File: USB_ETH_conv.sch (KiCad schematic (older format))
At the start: 20 parts

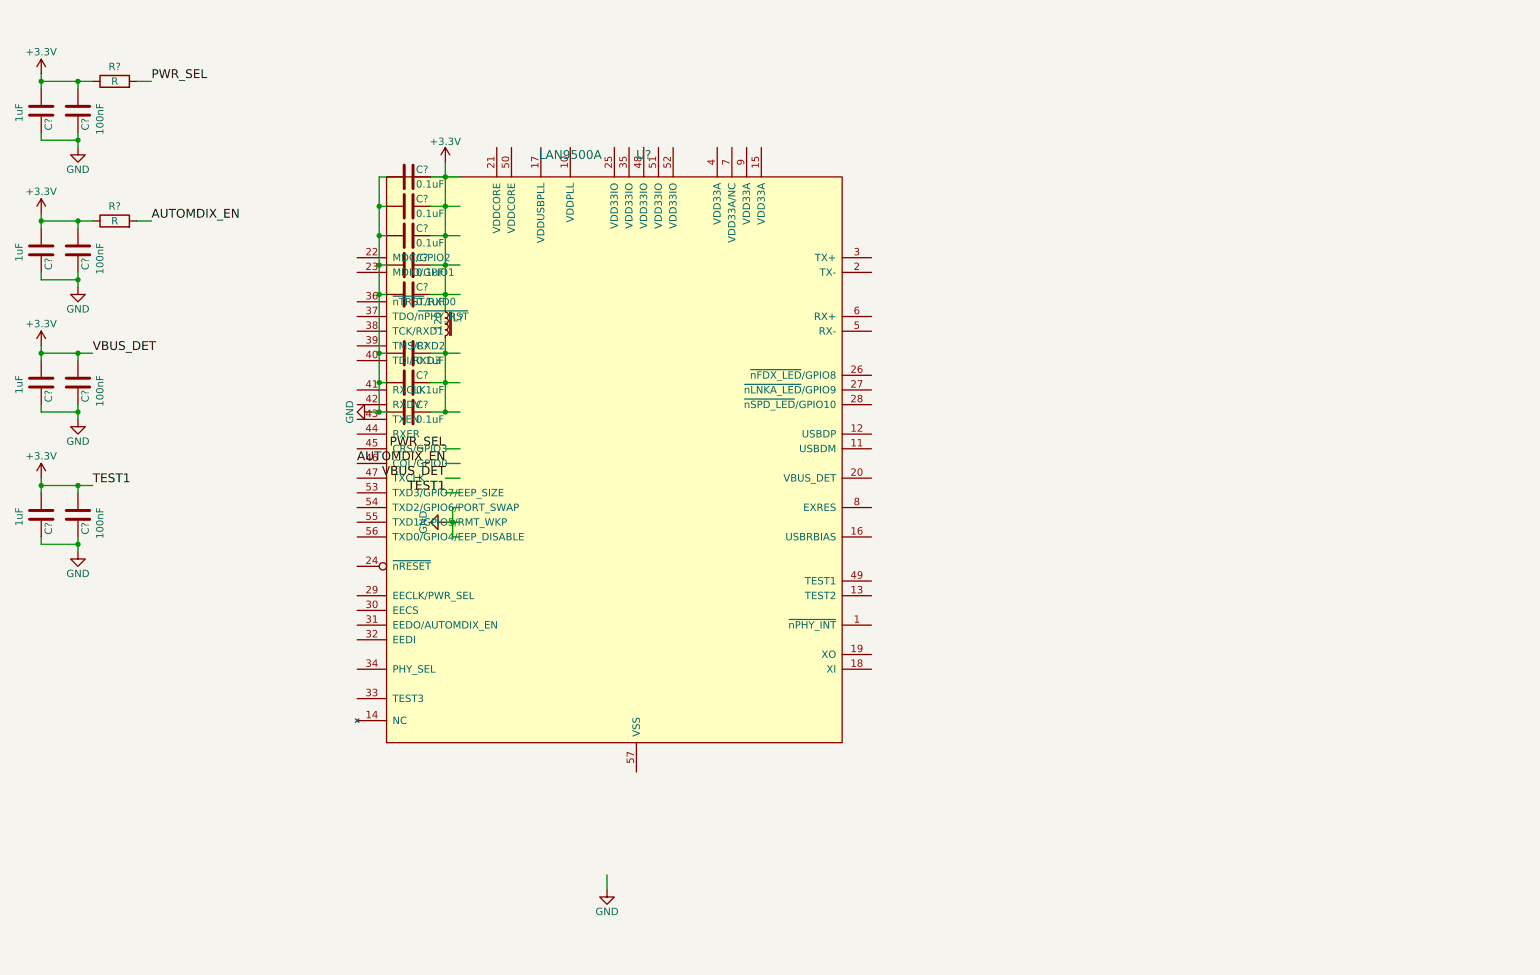
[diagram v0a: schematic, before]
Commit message: Finished LAN9500A ETH to USB interface sheet.
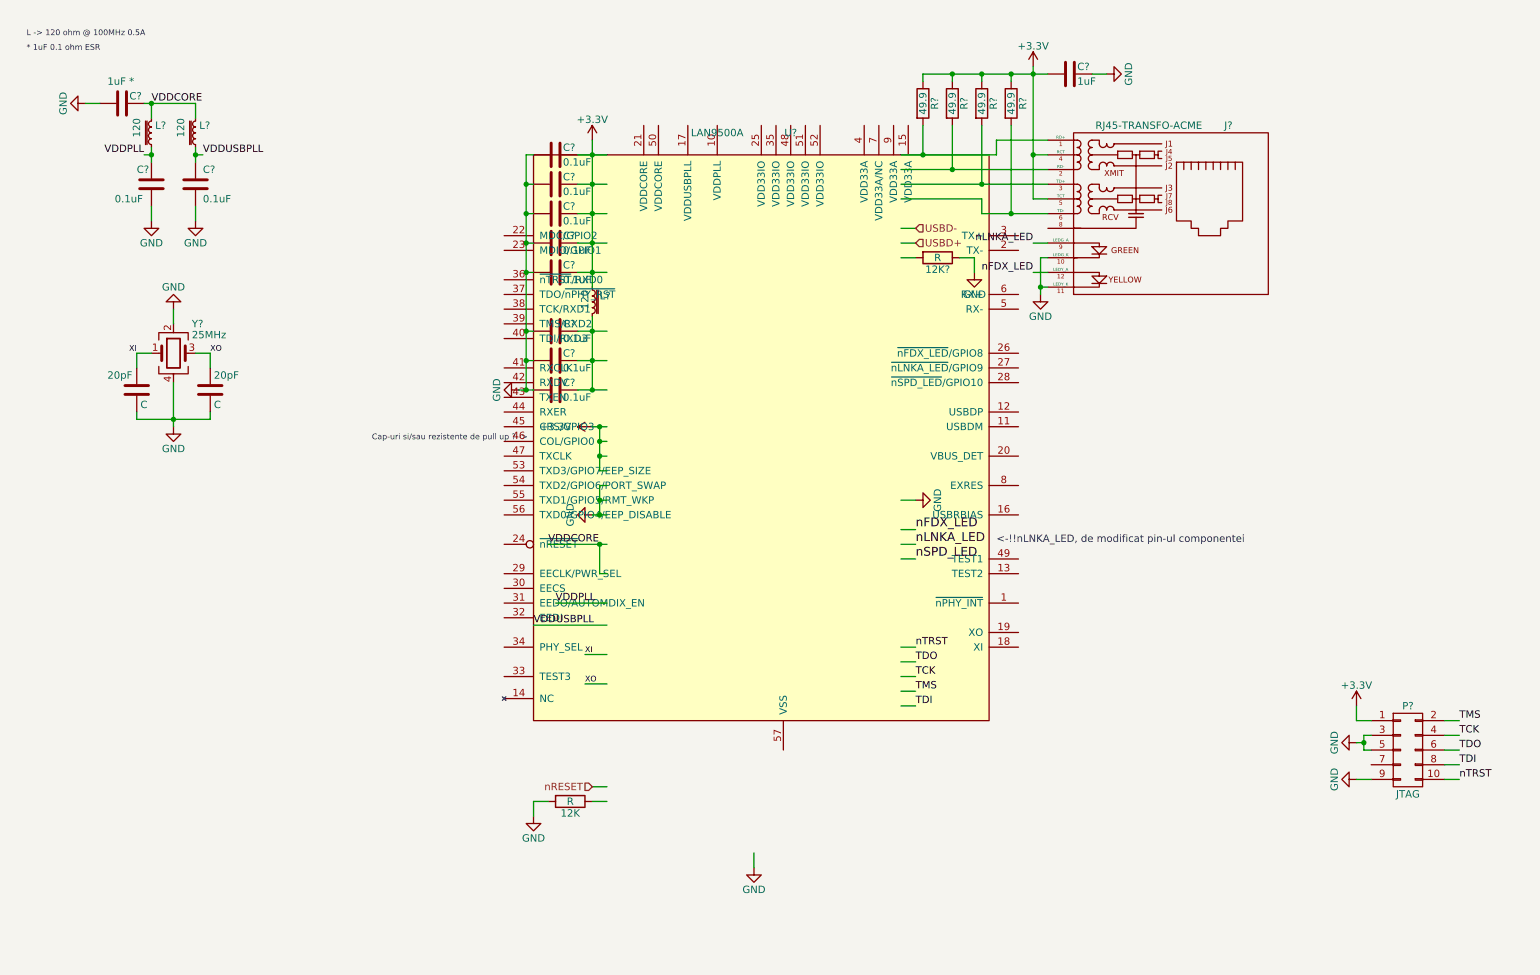
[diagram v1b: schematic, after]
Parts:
- removed C? (x4): 100nF, symbol C
- removed C? (x4): 1uF, symbol C
- removed R? (x2): R, symbol R
- added 12K, 12K?: R, symbol R
- added 20pF (x2): C, symbol C
- added C?: 1uF *, symbol C
- added C? (x2): 0.1uF, symbol C
- added C?: 1uF, symbol C
- added J?: RJ45-TRANSFO-ACME, symbol RJ45-TRANSFO-ACME
- added L? (x2): 120, symbol L_Core_Iron_Small
- added P?: JTAG, symbol CONN_02X05
- added R? (x4): 49.9, symbol R
- added Y?: 25MHz, symbol Crystal_GND24
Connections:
- net labels added: TCK, TDI, TDO, TMS, USBD+, USBD-, VDDCORE, VDDPLL, VDDUSBPLL, XI, XO, nFDX_LED, nLNKA_LED, nRESET, nSPD_LED, nTRST
- net labels removed: AUTOMDIX_EN, PWR_SEL, TEST1, VBUS_DET
- wire segments 54 -> 111
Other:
- note added: "* 1uF 0.1 ohm ESR"
- note added: "<-!!nLNKA_LED, de modificat pin-ul componentei"
- note added: "Cap-uri si/sau rezistente de pull up ? ->"
- note added: "L -> 120 ohm @ 100MHz 0.5A"
- moved on the sheet: C?, L?, U?

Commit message: Schematic correction
Corrected the direction on some signals. Added a pin header for general development.
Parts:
- 12K1: renamed from 12K; footprint (none) -> Resistors_SMD:R_0603_HandSoldering
- 12K2: renamed from 12K?; footprint (none) -> Resistors_SMD:R_0603_HandSoldering
- 20pF1, 20pF2: renamed from 20pF; footprint (none) -> Capacitors_SMD:C_0603_HandSoldering
- C25, C26, C27, C28, C29, C30, C31, C32, C33, C34, C35, C36: renamed from C?; footprint (none) -> Capacitors_SMD:C_0603_HandSoldering
- R6, R7, R8, R9: renamed from R?; footprint (none) -> Resistors_SMD:R_0603_HandSoldering
- gave numbers to parts that had none: 7

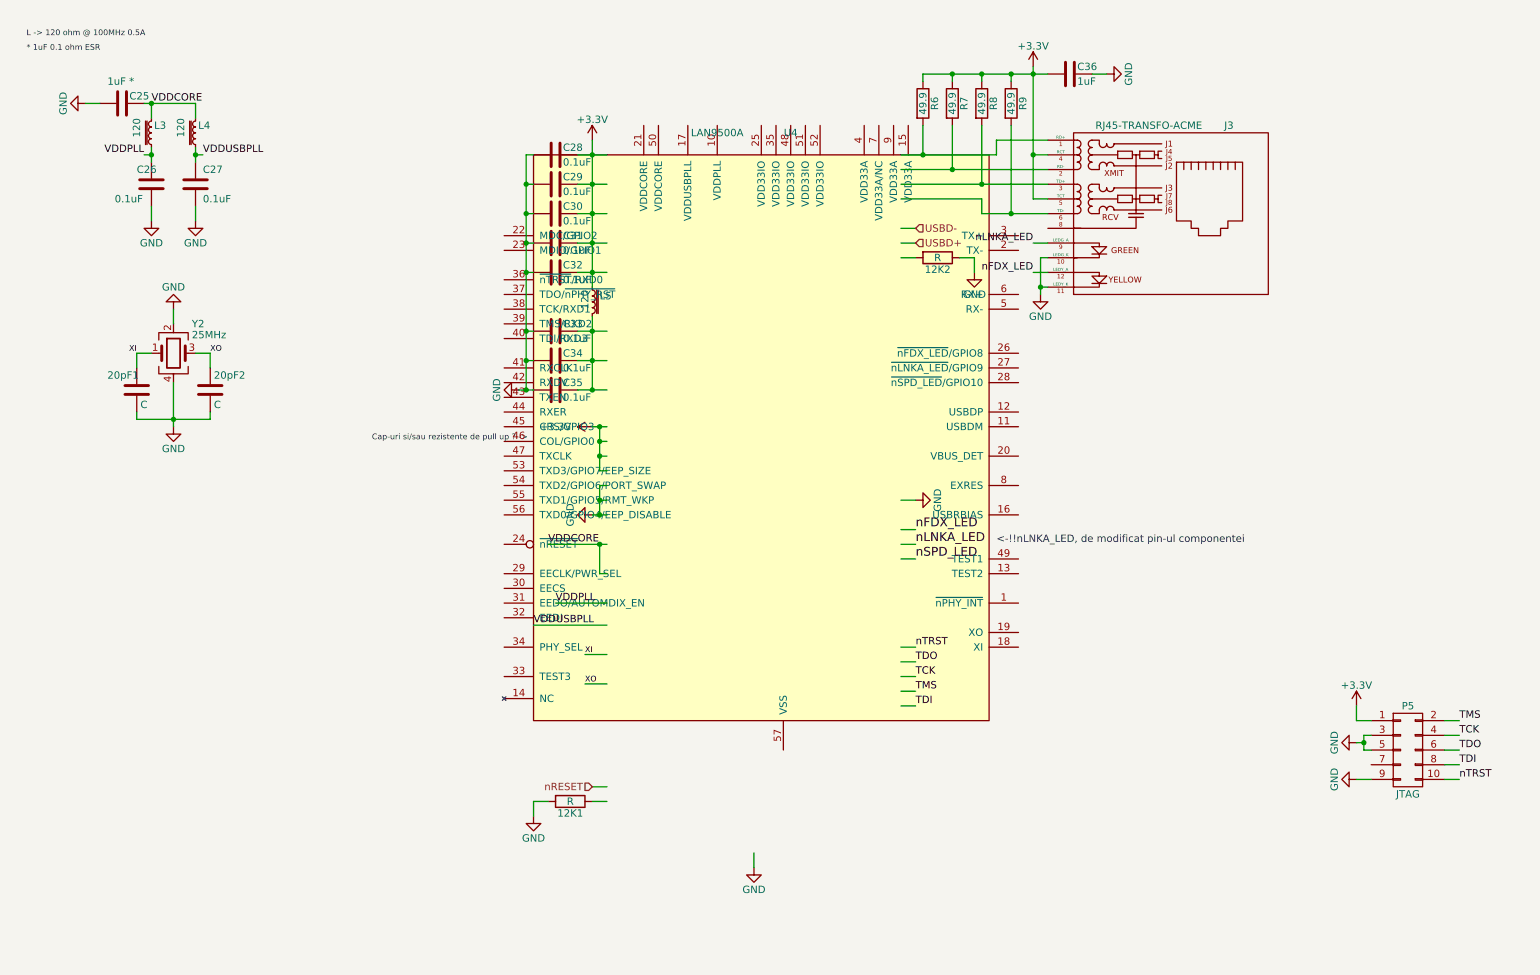
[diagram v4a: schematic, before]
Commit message: Modified LAN9500A schematic.
Modified the schematic for the USB to Ethernet converter.
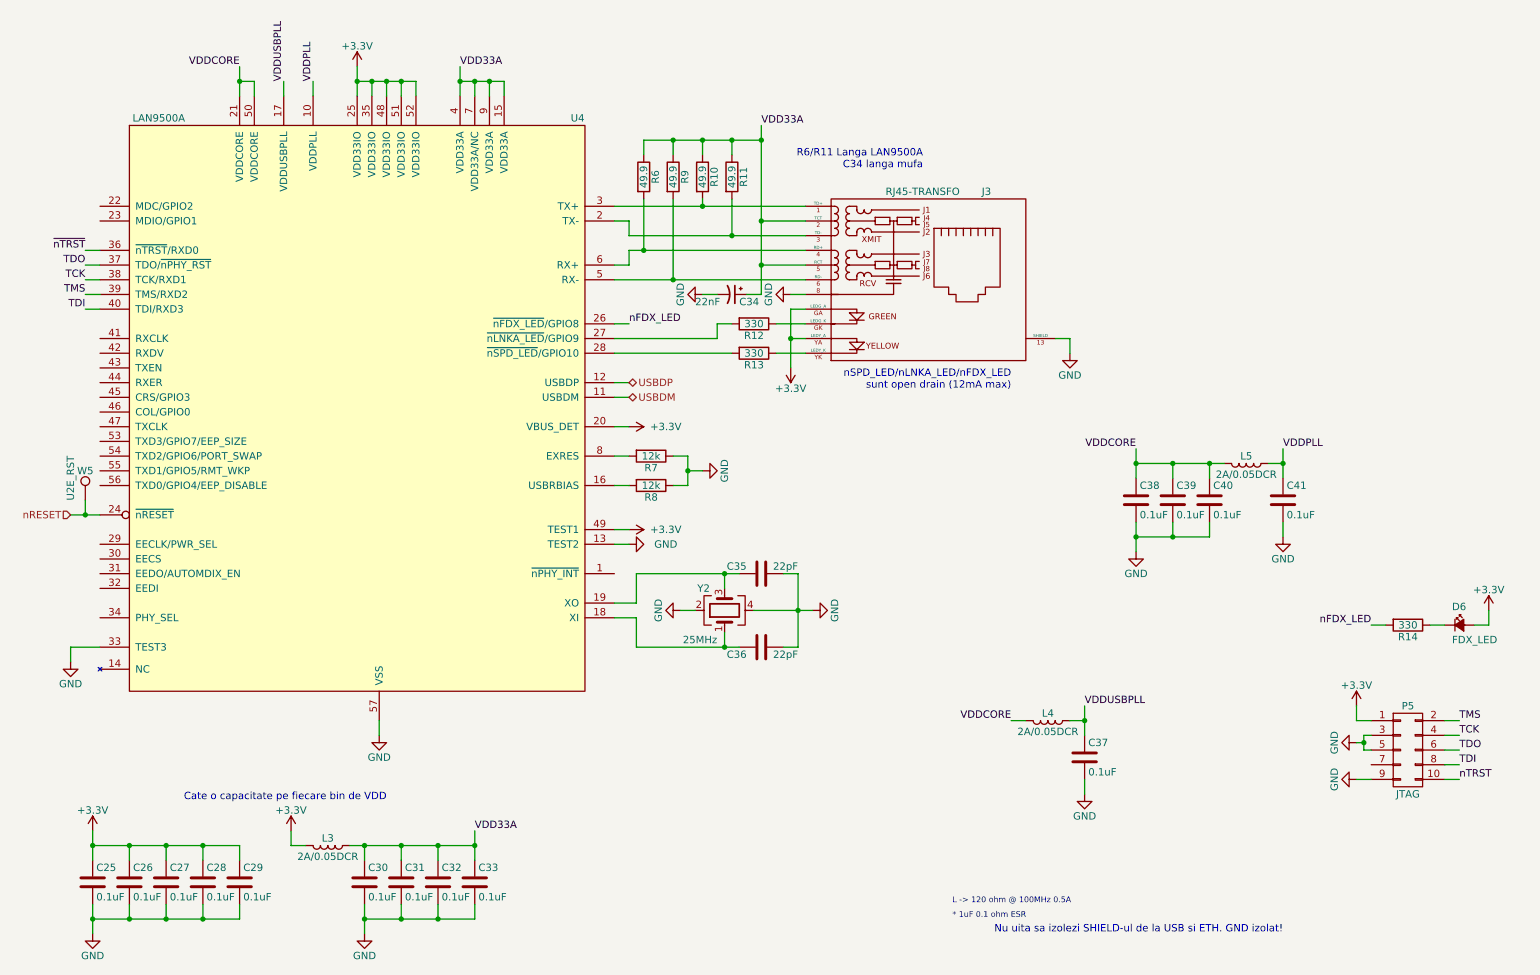
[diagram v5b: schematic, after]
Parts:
- removed 12K1, 12K2: R, Resistors_SMD:R_0603_HandSoldering, symbol R
- removed 20pF1, 20pF2: C, Capacitors_SMD:C_0603_HandSoldering, symbol C
- removed C34: 0.1uF, Capacitors_SMD:C_0603_HandSoldering, symbol C
- removed J3: RJ45-TRANSFO-ACME, symbol RJ45-TRANSFO-ACME
- removed L3, L4, L5: 120, symbol L_Core_Iron_Small
- added C34: 22nF, Capacitors_SMD:C_0805_HandSoldering, symbol CP1_Small
- added C37, C38, C39, C40, C41: 0.1uF, Capacitors_SMD:C_0805_HandSoldering, symbol C
- added D6: FDX_LED, LEDs:LED_0805, symbol LED_Small_ALT
- added J3: RJ45-TRANSFO, Connectors:RJ45_TRANSFO, symbol RJ45-TRANSFO
- added L3, L4, L5: 2A/0.05DCR, symbol L
- added R10, R11: 49.9, Resistors_SMD:R_0805_HandSoldering, symbol R
- added R12, R13, R14: 330, Resistors_SMD:R_0805_HandSoldering, symbol R
- added W5: U2E_RST, symbol TEST_1P
- C25: value 1uF * -> 0.1uF; footprint Capacitors_SMD:C_0603_HandSoldering -> Capacitors_SMD:C_0805_HandSoldering
- C26, C27, C28, C29, C30, C31, C32, C33: footprint Capacitors_SMD:C_0603_HandSoldering -> Capacitors_SMD:C_0805_HandSoldering
- C35: value 0.1uF -> 22pF; footprint Capacitors_SMD:C_0603_HandSoldering -> Capacitors_SMD:C_0805_HandSoldering
- C36: value 1uF -> 22pF; footprint Capacitors_SMD:C_0603_HandSoldering -> Capacitors_SMD:C_0805_HandSoldering
- R6, R9: footprint Resistors_SMD:R_0603_HandSoldering -> Resistors_SMD:R_0805_HandSoldering
- R7, R8: value 49.9 -> 12k; footprint Resistors_SMD:R_0603_HandSoldering -> Resistors_SMD:R_0805_HandSoldering
- Y2: footprint (none) -> Crystals:Crystal_SMD_3225-4pin_3.2x2.5mm_HandSoldering
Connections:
- net labels added: USBDM, USBDP, VDD33A, ~nTRST
- net labels removed: USBD+, USBD-, XI, XO, nLNKA_LED, nSPD_LED
- wire segments 111 -> 140
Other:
- note added: "Cate o capacitate pe fiecare bin de VDD"
- note added: "Nu uita sa izolezi SHIELD-ul de la USB si ETH. GND izolat!"
- note added: "R6/R11 Langa LAN9500A\nC34 langa mufa"
- note added: "nSPD_LED/nLNKA_LED/nFDX_LED\nsunt open drain (12mA max)"
- note removed: "<-!!nLNKA_LED, de modificat pin-ul componentei"
- note removed: "Cap-uri si/sau rezistente de pull up ? ->"
- moved on the sheet: U4

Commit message: Schematic changes. PCB in process of making.
Removed LAN9500A Jtag. Removed Aria G25 pinout. Removed USB connectors. Added rezistors to USB/ETH/ySD shields.
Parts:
- removed P5: JTAG, symbol CONN_02X05
- added R20: 1M, Resistors_SMD:R_0805_HandSoldering, symbol R
- C25, C26, C27, C28, C29, C30, C31, C32, C33, C35, C36, C37, C38, C39, C40, C41: footprint Capacitors_SMD:C_0805_HandSoldering -> Capacitors_SMD:C_0603_HandSoldering
- L3, L4, L5: footprint (none) -> Resistors_SMD:R_0603_HandSoldering
- R7, R8: footprint Resistors_SMD:R_0805_HandSoldering -> Resistors_SMD:R_0603_HandSoldering
- U4: footprint (none) -> Housings_DFN_QFN:QFN-56-1EP_7x7mm_Pitch0.4mm
- W5: footprint (none) -> Measurement_Points:Measurement_Point_Round-SMD-Pad_Small
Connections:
- net GND: now also R20.1; no longer J3.13 (SHIELD)
- net TX-: now reaches J3.3 (TD-), R11.2, U4.2 (TX-)
- net TX+: now reaches J3.1 (TD+), R10.2, U4.3 (TX+)
- net RX-: now reaches J3.6 (RD-), R9.2, U4.5 (RX-)
- net RX+: now reaches J3.4 (RD+), R6.2, U4.6 (RX+)
- new net: J3.13 (SHIELD), R20.2

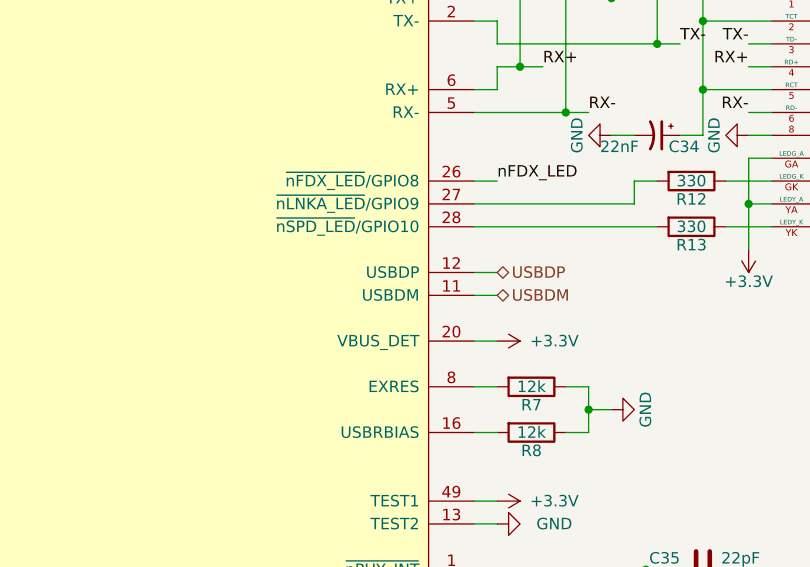
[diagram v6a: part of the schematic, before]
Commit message: Modified USB/ETH label names.
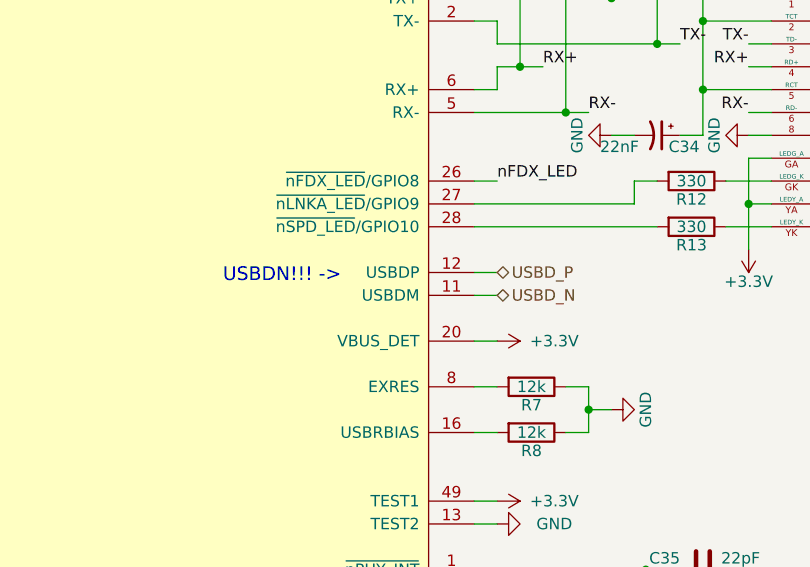
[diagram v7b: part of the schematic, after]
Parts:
- D6: footprint LEDs:LED_0805 -> LEDs:LED_0603
- R10, R11, R12, R13, R14, R20, R6, R9: footprint Resistors_SMD:R_0805_HandSoldering -> Resistors_SMD:R_0603_HandSoldering
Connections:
- net USBDM renamed USBD_N
- net USBDP renamed USBD_P
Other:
- note added: "USBDN!!! ->"
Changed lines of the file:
@@
 F 0 "R6" V 5030 1700 50  0000 C CNN
 F 1 "49.9" V 4950 1700 50  0000 C CNN
-F 2 "Resistors_SMD:R_0805_HandSoldering" V 4880 1700 50  0001 C CNN
+F 2 "Resistors_SMD:R_0603_HandSoldering" V 4880 1700 50  0001 C CNN
 F 3 "" H 4950 1700 50  0000 C CNN
 	1    4950 1700
@@
 F 0 "R9" V 5230 1700 50  0000 C CNN
 F 1 "49.9" V 5150 1700 50  0000 C CNN
-F 2 "Resistors_SMD:R_0805_HandSoldering" V 5080 1700 50  0001 C CNN
+F 2 "Resistors_SMD:R_0603_HandSoldering" V 5080 1700 50  0001 C CNN
 F 3 "" H 5150 1700 50  0000 C CNN
 	1    5150 1700
@@
 F 0 "R10" V 5430 1700 50  0000 C CNN
 F 1 "49.9" V 5350 1700 50  0000 C CNN
-F 2 "Resistors_SMD:R_0805_HandSoldering" V 5280 1700 50  0001 C CNN
+F 2 "Resistors_SMD:R_0603_HandSoldering" V 5280 1700 50  0001 C CNN
 F 3 "" H 5350 1700 50  0000 C CNN
 	1    5350 1700
@@
 F 0 "R12" V 5780 2700 50  0000 C CNN
 F 1 "330" V 5700 2700 50  0000 C CNN
-F 2 "Resistors_SMD:R_0805_HandSoldering" V 5630 2700 50  0001 C CNN
+F 2 "Resistors_SMD:R_0603_HandSoldering" V 5630 2700 50  0001 C CNN
 F 3 "" H 5700 2700 50  0000 C CNN
 	1    5700 2700
@@
 F 0 "R13" V 5780 2900 50  0000 C CNN
 F 1 "330" V 5700 2900 50  0000 C CNN
-F 2 "Resistors_SMD:R_0805_HandSoldering" V 5630 2900 50  0001 C CNN
+F 2 "Resistors_SMD:R_0603_HandSoldering" V 5630 2900 50  0001 C CNN
 F 3 "" H 5700 2900 50  0000 C CNN
 	1    5700 2900
@@
 F 0 "R14" V 10230 4750 50  0000 C CNN
 F 1 "330" V 10150 4750 50  0000 C CNN
-F 2 "Resistors_SMD:R_0805_HandSoldering" V 10080 4750 50  0001 C CNN
+F 2 "Resistors_SMD:R_0603_HandSoldering" V 10080 4750 50  0001 C CNN
 F 3 "" H 10150 4750 50  0000 C CNN
 	1    10150 4750
@@
 F 0 "D6" H 10450 4875 50  0000 L CNN
 F 1 "FDX_LED" H 10450 4650 50  0000 L CNN
-F 2 "LEDs:LED_0805" V 10500 4750 50  0001 C CNN
+F 2 "LEDs:LED_0603" V 10500 4750 50  0001 C CNN
 F 3 "" V 10500 4750 50  0000 C CNN
 	1    10500 4750
@@
 $EndComp
 Text HLabel 4850 3100 2    50   BiDi ~ 0
-USBDP
+USBD_P
 Text HLabel 4850 3200 2    50   BiDi ~ 0
-USBDM
+USBD_N
 $Comp
 L R R7
@@
 F 0 "R11" V 5630 1700 50  0000 C CNN
 F 1 "49.9" V 5550 1700 50  0000 C CNN
-F 2 "Resistors_SMD:R_0805_HandSoldering" V 5480 1700 50  0001 C CNN
+F 2 "Resistors_SMD:R_0603_HandSoldering" V 5480 1700 50  0001 C CNN
 F 3 "" H 5550 1700 50  0000 C CNN
 	1    5550 1700
@@
 F 0 "R20" V 8080 2800 50  0000 C CNN
 F 1 "1M" V 8000 2800 50  0000 C CNN
-F 2 "Resistors_SMD:R_0805_HandSoldering" V 7930 2800 50  0001 C CNN
+F 2 "Resistors_SMD:R_0603_HandSoldering" V 7930 2800 50  0001 C CNN
 F 3 "" H 8000 2800 50  0000 C CNN
 	1    8000 2800
@@
 Wire Wire Line
 	5950 2400 6050 2400
+Text Notes 3650 3150 0    60   ~ 0
+USBDN!!! ->
 $EndSCHEMATC
